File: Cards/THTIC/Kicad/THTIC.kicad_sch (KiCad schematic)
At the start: 38 parts, among them J1 Conn_01x04_Pin, J2 Plasma 300V, J3 Plasma 300V, U1 B0509S-1WR3, U2 ISO1540, U3 MCP3221, U4 MCP3221, U5 LMV321, U6 AMS1117-5, U7 LMV321

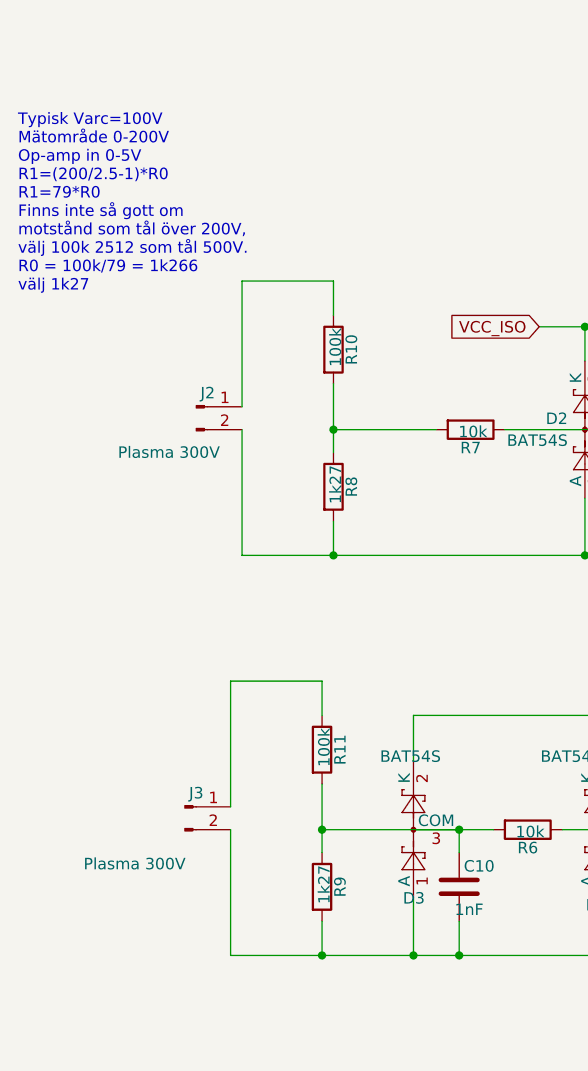
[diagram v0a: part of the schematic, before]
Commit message: Works in TwinCAT. Prepare for test in machine.
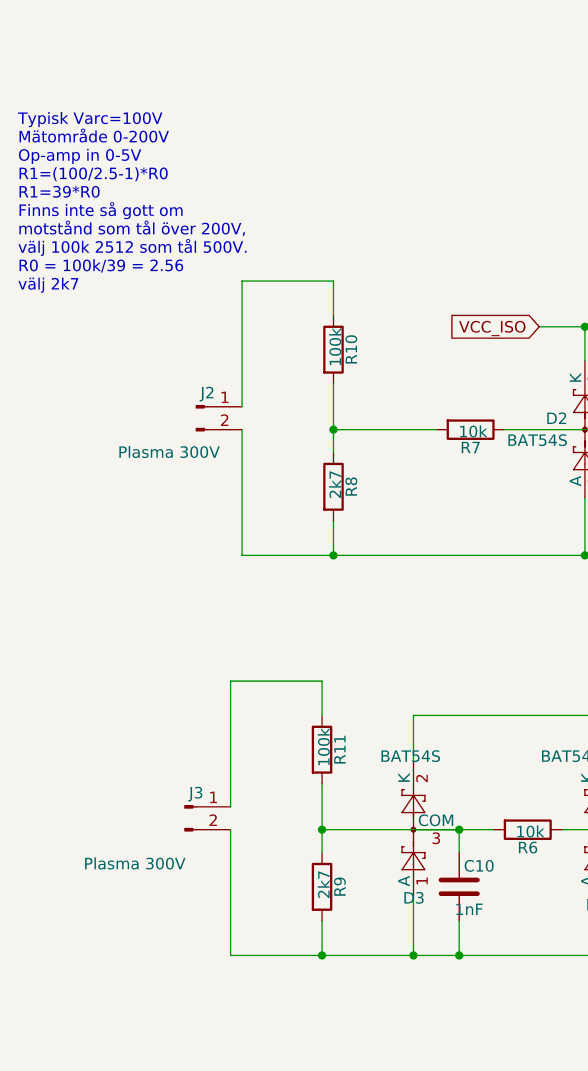
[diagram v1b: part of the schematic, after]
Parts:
- R8, R9: value 1k27 -> 2k7
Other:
- note added: "Typisk Varc=100V Mätområde 0-200V Op-amp in 0-5V R1=(100/2.5-1)*R0 R1=39*R0 Finns inte så gott om motstånd som tål över 200V, välj 100k 2512 som tål 500V. R0 = 100k/39 = 2.56 välj 2k7"
- note removed: "Typisk Varc=100V Mätområde 0-200V Op-amp in 0-5V R1=(200/2.5-1)*R0 R1=79*R0 Finns inte så gott om motstånd som tål över 200V, välj 100k 2512 som tål 500V. R0 = 100k/79 = 1k266 välj 1k27"
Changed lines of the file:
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@@
 		)
 	)
-	(text "Typisk Varc=100V\nMätområde 0-200V\nOp-amp in 0-5V\nR1=(200/2.5-1)*R0\nR1=79*R0\nFinns inte så gott om\nmotstånd som tål över 200V,\nvälj 100k 2512 som tål 500V.\nR0 = 100k/79 = 1k266\nvälj 1k27"
+	(text "Typisk Varc=100V\nMätområde 0-200V\nOp-amp in 0-5V\nR1=(100/2.5-1)*R0\nR1=39*R0\nFinns inte så gott om\nmotstånd som tål över 200V,\nvälj 100k 2512 som tål 500V.\nR0 = 100k/39 = 2.56\nvälj 2k7"
 		(exclude_from_sim no)
 		(at 17.018 41.148 0)
@@
 			)
 		)
-		(property "Value" "1k27"
+		(property "Value" "2k7"
 			(at 52.324 82.296 90)
 			(effects
@@
 			)
 		)
-		(property "Value" "1k27"
+		(property "Value" "2k7"
 			(at 51.054 126.746 90)
 			(effects

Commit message: Ordered the real version
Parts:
- removed C10: 1nF, Capacitor_SMD:C_0603_1608Metric, symbol Device:C
- removed C3: 100nF, Capacitor_SMD:C_0603_1608Metric, symbol Device:C
- removed C5, C7: nP, Capacitor_SMD:C_0603_1608Metric, symbol Device:C
- removed D1: BAT54S/nP, Package_TO_SOT_SMD:SOT-23, symbol Diode:BAT54S
- removed D3: BAT54S, Package_TO_SOT_SMD:SOT-23, symbol Diode:BAT54S
- removed J3: Plasma 300V, Connector_Phoenix_MC:PhoenixContact_MCV_1,5_2-G-3.5_1x02_P3.50mm_Vertical, symbol Connector:Conn_01x02_Pin
- removed R11: 100k, Resistor_SMD:R_2512_6332Metric, symbol Device:R
- removed R4, R6: 10k, Resistor_SMD:R_0603_1608Metric, symbol Device:R
- removed R9: 2k7, Resistor_SMD:R_0603_1608Metric, symbol Device:R
- removed U3: MCP3221, Package_TO_SOT_SMD:SOT-23-5, symbol HakansLibrary:MCP3221
- removed U5: LMV321, Package_TO_SOT_SMD:SOT-23-5, symbol Amplifier_Operational:LMV321
- added R1: 2k2, Resistor_SMD:R_0805_2012Metric, symbol Device:R
- C1: footprint Capacitor_SMD:C_0603_1608Metric -> Capacitor_SMD:C_0805_2012Metric
- C3: renamed from C4; footprint Capacitor_SMD:C_0603_1608Metric -> Capacitor_SMD:C_0805_2012Metric
- C4: renamed from C6; footprint Capacitor_SMD:C_0603_1608Metric -> Capacitor_SMD:C_0805_2012Metric
- C5: renamed from C9; footprint Capacitor_SMD:C_0603_1608Metric -> Capacitor_SMD:C_0805_2012Metric
- R2: value 47 -> 2k2; footprint Resistor_SMD:R_0603_1608Metric -> Resistor_SMD:R_0805_2012Metric
- R3, R5, R8: footprint Resistor_SMD:R_0603_1608Metric -> Resistor_SMD:R_0805_2012Metric
- R4: renamed from R1; footprint Resistor_SMD:R_0603_1608Metric -> Resistor_SMD:R_0805_2012Metric
- R6: renamed from R7; footprint Resistor_SMD:R_0603_1608Metric -> Resistor_SMD:R_0805_2012Metric
- renumbered C8 to C6, D2 to D1, R10 to R7, U4 to U3, U6 to U4, U7 to U5
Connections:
- net 5V: now also R2.1, R1.1
- net at J1.2 (Pin_2), U2.2 (SDA1): now also R2.2
- net at J1.3 (Pin_3), U2.3 (SCL1): now also R1.2
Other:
- note added: "Isolation voltage 1.5 kV"
- note added: "Isolation voltage 2.5 kV"
- note added: "Optional I2C pullups Weaker pullups on both sides can help noise"
- note added: "Typical Varc=100V Range 0-200V Op-amp range 0-5V R1=(200/5-1)*R0 R1=39*R0 Limited assortment of resistors that can handle 200V+, choose 100k 2512, allowed 500V. R0 = 100k/39 = 2.56k choose 2k7 Will need calibration anyway"
- note removed: "Typisk Varc=100V Mätområde 0-200V Op-amp in 0-5V R1=(100/2.5-1)*R0 R1=39*R0 Finns inte så gott om motstånd som tål över 200V, välj 100k 2512 som tål 500V. R0 = 100k/39 = 2.56 välj 2k7"
- moved on the sheet: C5, D1, J1, J2, R3, R4, R5, R6, R7, R8, U5

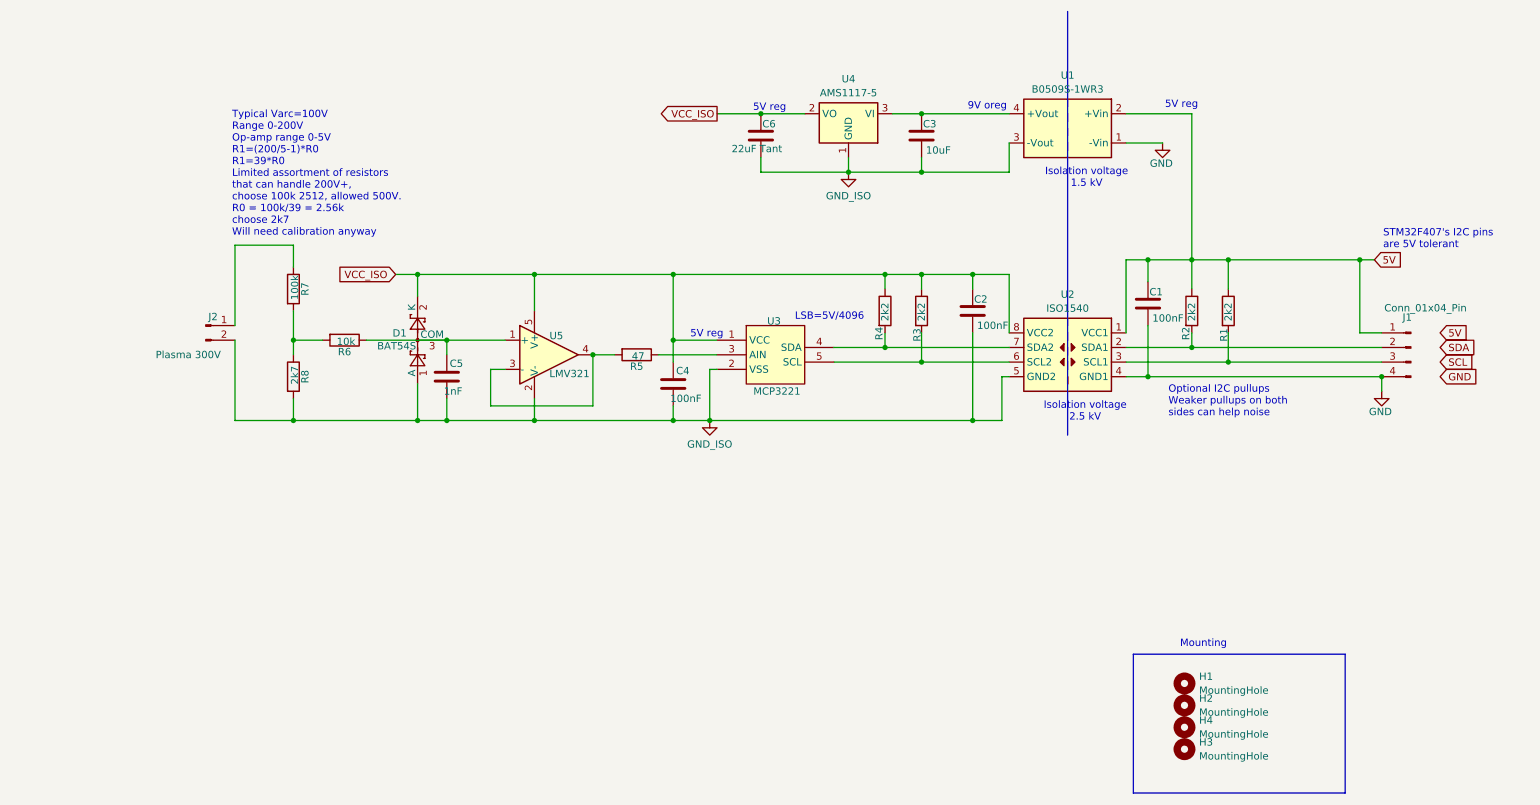
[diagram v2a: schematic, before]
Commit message: Now measuring 0 - -200 Volts.
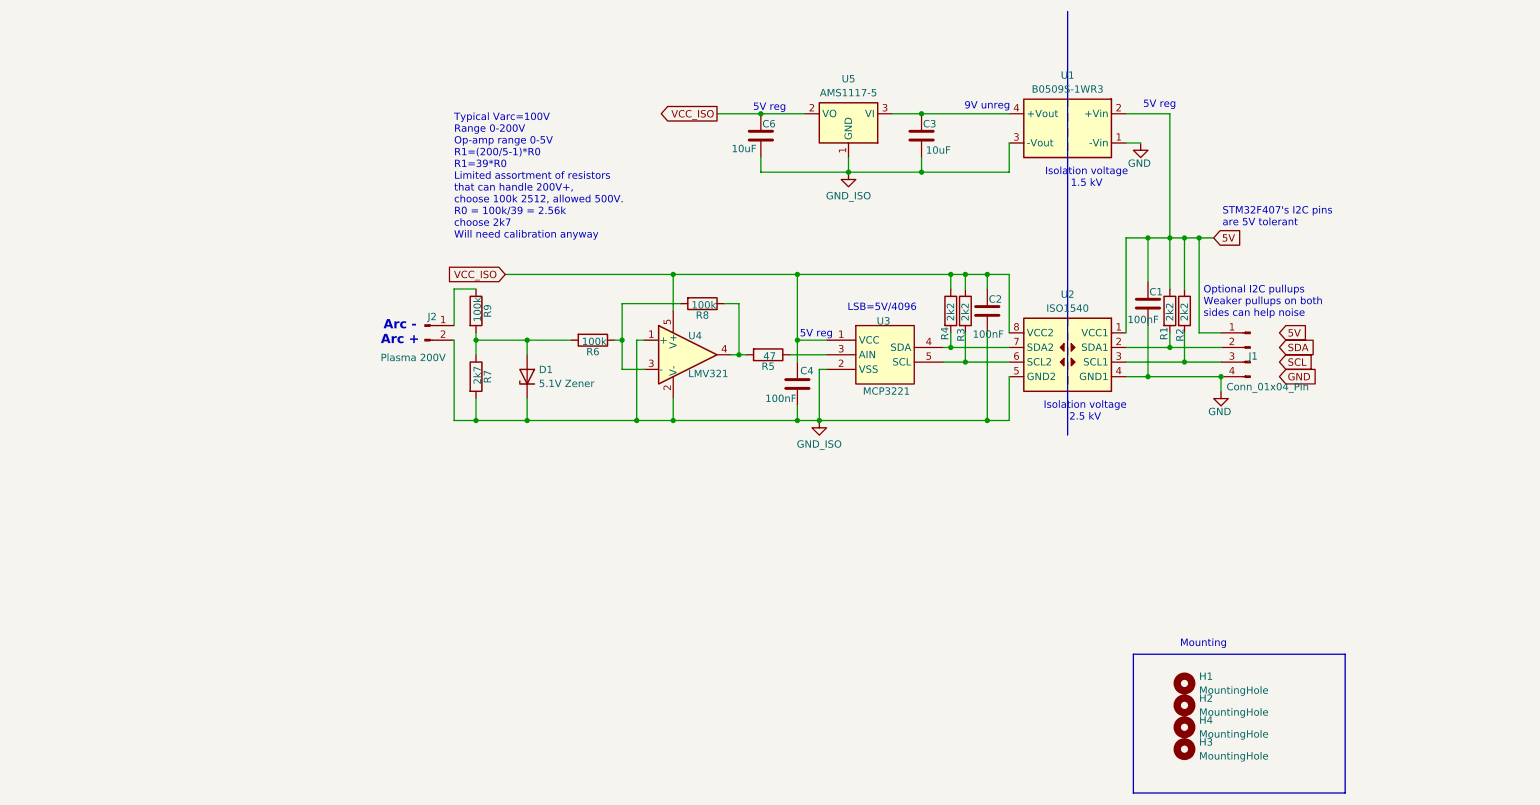
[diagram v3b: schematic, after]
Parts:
- removed C5: 1nF, Capacitor_SMD:C_0805_2012Metric, symbol Device:C
- removed D1: BAT54S, Package_TO_SOT_SMD:SOT-23, symbol Diode:BAT54S
- added D1: 5.1V Zener, symbol Device:D_Zener
- added R8: 100k, Resistor_SMD:R_0805_2012Metric, symbol Device:R
- C6: value 22uF Tant -> 10uF
- J2: value Plasma 300V -> Plasma 200V
- R6: value 10k -> 100k
- renumbered R2 to R1, R1 to R2, R8 to R7, R7 to R9, U5 to U4, U4 to U5
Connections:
- net GND_ISO: now also U4.1 (+), D1.1 (K)
- net at R6.2, R7.1, R9.2: now also D1.2 (A)
- net at R6.1: now also U4.3 (-), R8.2; no longer U4.1 (+)
- net at R5.2, U4.4: now also R8.1; no longer U4.3 (-)
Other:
- note added: "9V unreg"
- note added: "Arc - Arc +"
- note removed: "9V oreg"
- moved on the sheet: C2, C4, J1, J2, R1, R2, R3, R4, R5, R7, R9, U3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

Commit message: now saved
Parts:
- D1: footprint (none) -> Diode_SMD:D_SOD-323_HandSoldering
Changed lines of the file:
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@@
 			)
 		)
-		(property "Footprint" ""
+		(property "Footprint" "Diode_SMD:D_SOD-323_HandSoldering"
 			(at 106.68 82.55 0)
 			(effects

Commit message: Gerbers done.
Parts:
- added C5: 100nF, Capacitor_SMD:C_0805_2012Metric, symbol Device:C
- D1: footprint Diode_SMD:D_SOD-323_HandSoldering -> (none)
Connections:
- net GND_ISO: now also C5.2
- net VCC_ISO: now also C5.1
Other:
- moved on the sheet: C4, D1, J2, R5, R6, R7, R8, R9, U4
